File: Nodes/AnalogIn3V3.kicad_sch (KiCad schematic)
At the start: 20 parts, among them T19 Conn_01x01, T20 Conn_01x01, U10 LM358BAIDR

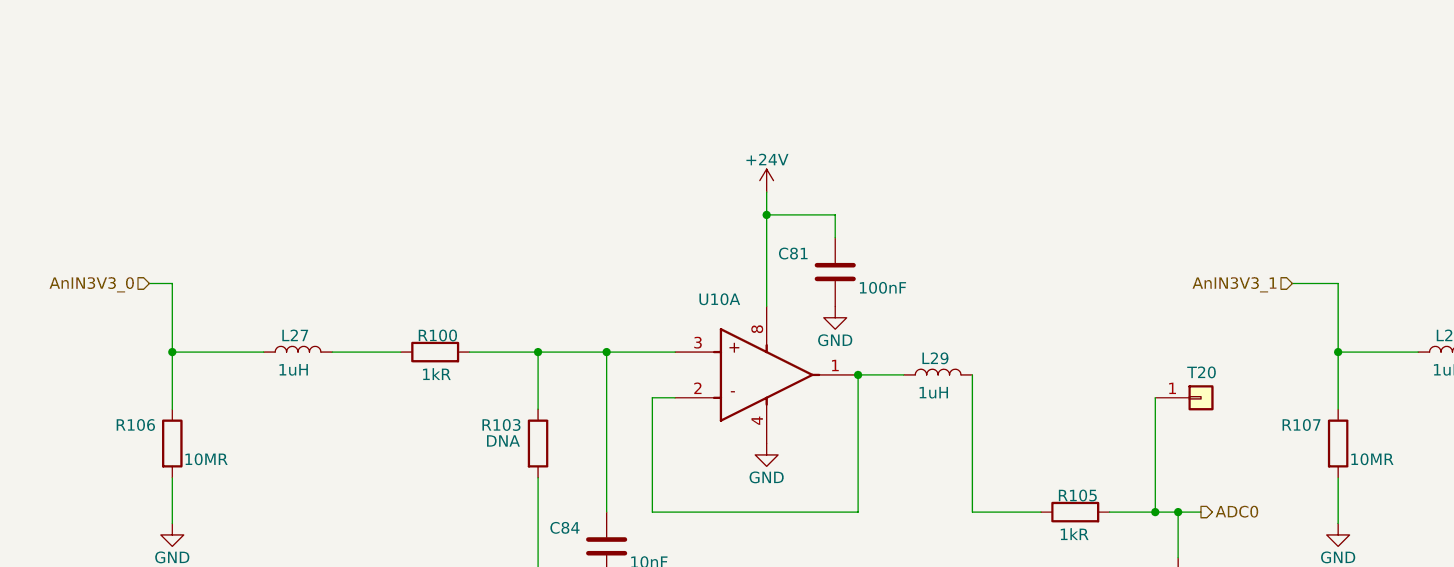
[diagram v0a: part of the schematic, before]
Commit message: Nodes v2.1.2 Improved
- Improved schematic design
- Added two 4.7 uF caps according to the datasheets of the microchips
- Other small changes
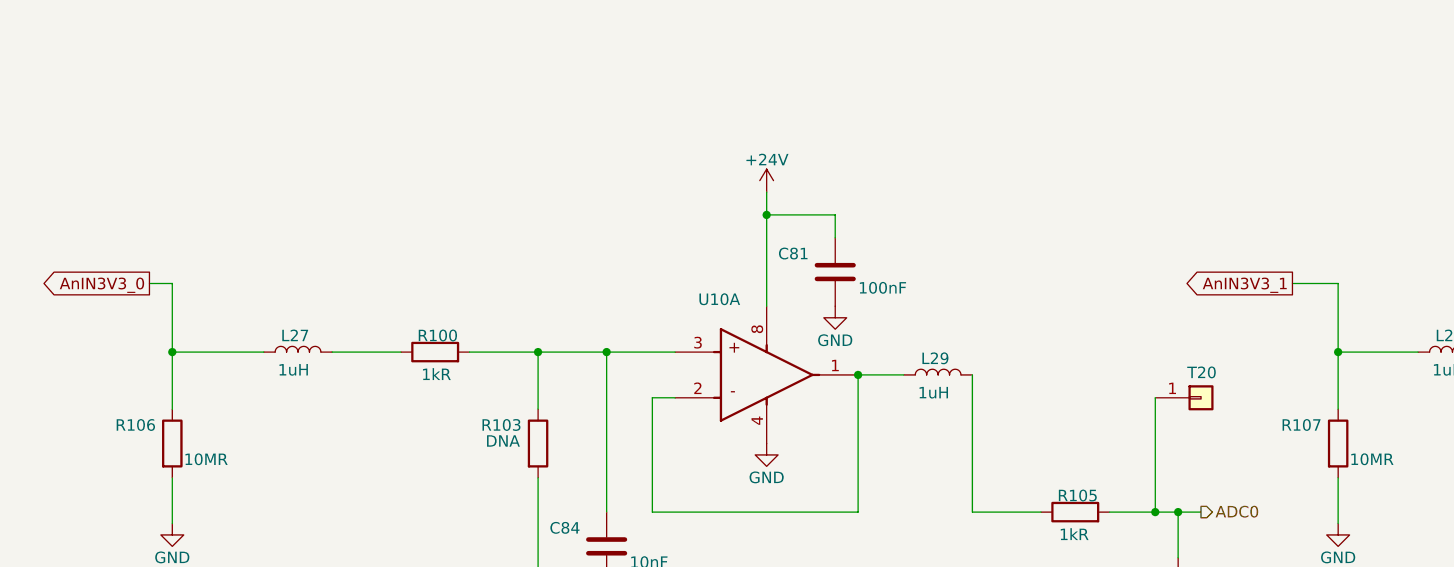
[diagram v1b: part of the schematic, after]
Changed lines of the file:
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@@
+		)
+	)
+	(global_label "AnIN3V3_1"
+		(shape output)
+		(at 151.13 62.23 180)
+		(fields_autoplaced yes)
+		(effects
+			(font
+				(size 1.27 1.27)
+			)
+			(justify right)
+		)
+		(property "Intersheetrefs" "${INTERSHEET_REFS}"
+			(at 138.2872 62.23 0)
+			(effects
+				(font
+					(size 1.27 1.27)
+				)
+				(justify right)
+				(hide yes)
+			)
+		)
+	)
+	(global_label "AnIN3V3_0"
+		(shape output)
+		(at 24.13 62.23 180)
+		(fields_autoplaced yes)
+		(effects
+			(font
+				(size 1.27 1.27)
+			)
+			(justify right)
+		)
+		(property "Intersheetrefs" "${INTERSHEET_REFS}"
+			(at 11.2872 62.23 0)
+			(effects
+				(font
+					(size 1.27 1.27)
+				)
+				(justify right)
+				(hide yes)
+			)
 		)
 	)
@@
 		)
 	)
-	(hierarchical_label "AnIN3V3_1"
-		(shape input)
-		(at 151.13 62.23 180)
-		(fields_autoplaced yes)
-		(effects
-			(font
-				(size 1.27 1.27)
-			)
-			(justify right)
-		)
-	)
-	(hierarchical_label "AnIN3V3_0"
-		(shape input)
-		(at 24.13 62.23 180)
-		(fields_autoplaced yes)
-		(effects
-			(font
-				(size 1.27 1.27)
-			)
-			(justify right)
-		)
-	)

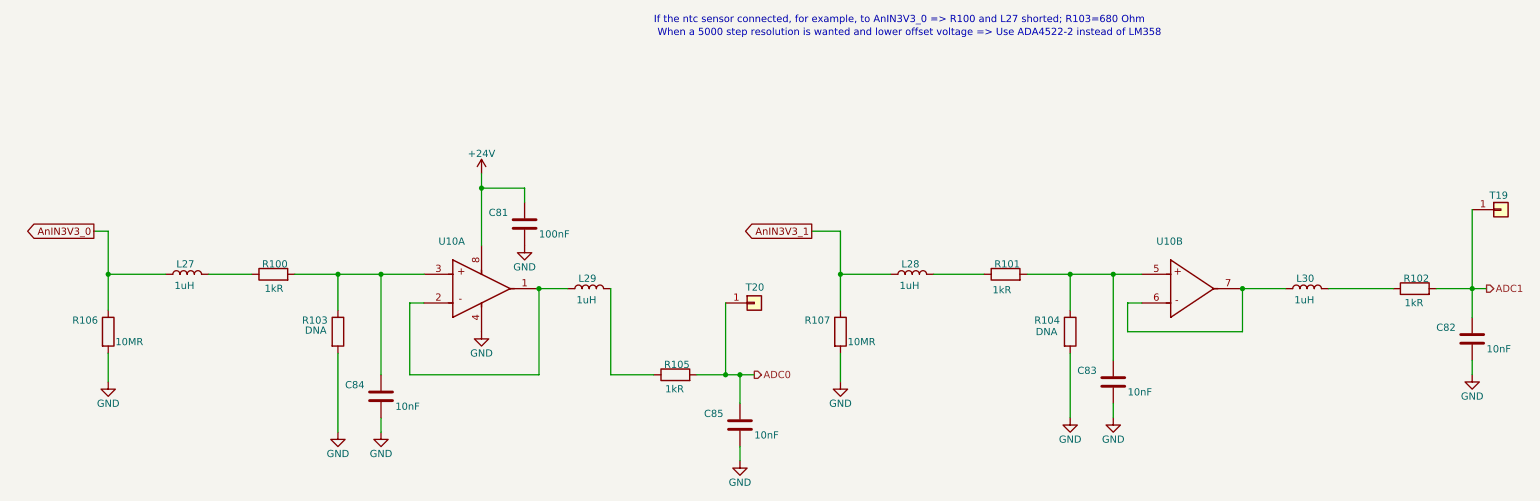
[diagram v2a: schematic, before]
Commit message: Nodes v2.2.5
- New High-Side Driver (Same footprint, just new info)
- Two resistors added for 3V3 Filters, which can be used to implement voltage divider
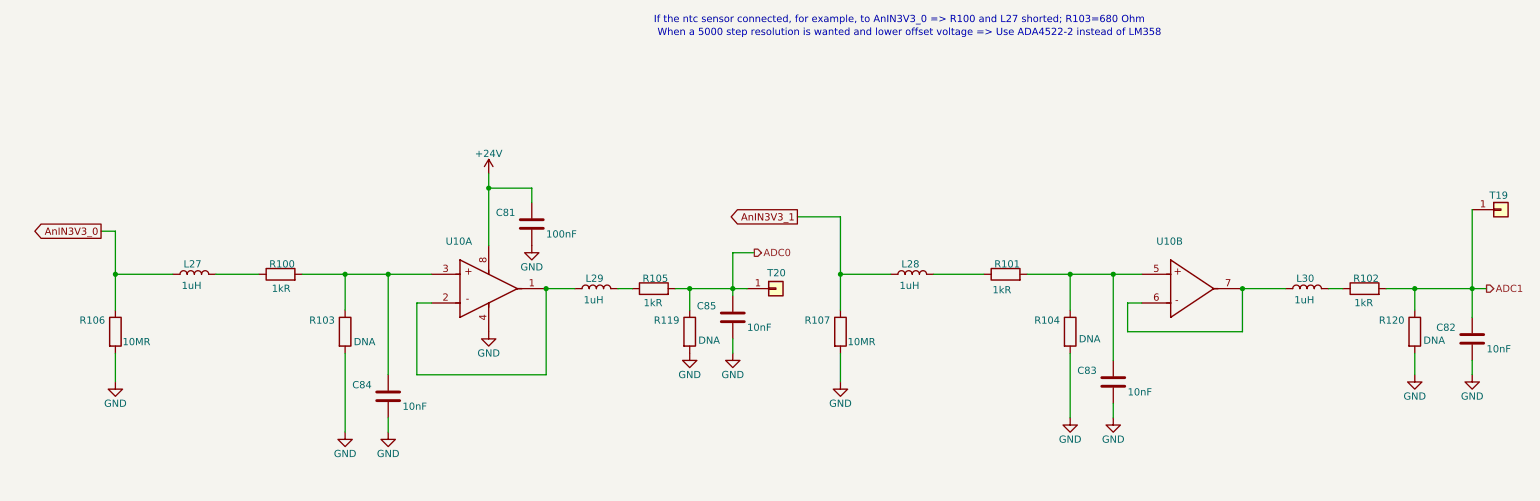
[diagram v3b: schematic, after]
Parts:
- added R119, R120: DNA, Resistor_SMD:R_0805_2012Metric_Pad1.20x1.40mm_HandSolder, symbol Device:R
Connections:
- net ADC0: now also R119.1
- net ADC1: now also R120.1
- net GND: now also R119.2, R120.2
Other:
- moved on the sheet: C81, C84, C85, L27, L29, R100, R102, R103, R105, R106, T20, U10A

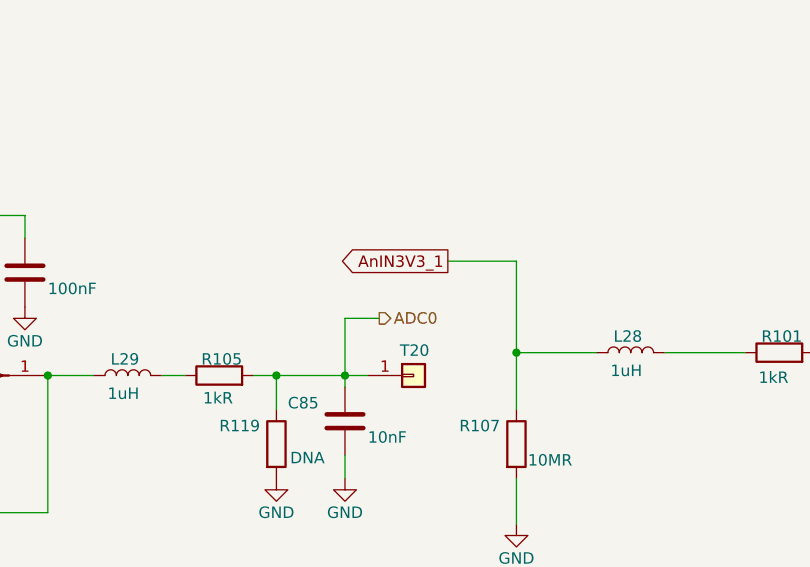
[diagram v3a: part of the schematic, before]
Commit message: Nodes 2.2.5 Revision 1
- New LED colour coding
- Nodes Datasheet added
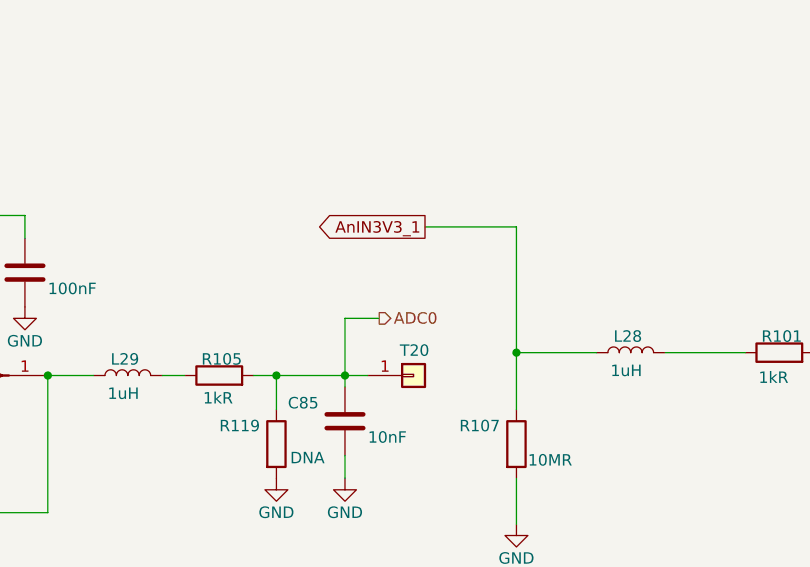
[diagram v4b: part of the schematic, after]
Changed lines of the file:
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@@
 	(wire
 		(pts
-			(xy 156.21 59.69) (xy 156.21 69.85)
+			(xy 156.21 55.88) (xy 156.21 69.85)
 		)
 		(stroke
@@
 	(wire
 		(pts
-			(xy 148.59 59.69) (xy 156.21 59.69)
+			(xy 146.05 55.88) (xy 156.21 55.88)
 		)
 		(stroke
@@
 	(global_label "AnIN3V3_1"
 		(shape output)
-		(at 148.59 59.69 180)
+		(at 146.05 55.88 180)
 		(fields_autoplaced yes)
 		(effects
@@
 		)
 		(property "Intersheetrefs" "${INTERSHEET_REFS}"
-			(at 135.7472 59.69 0)
+			(at 133.2072 55.88 0)
 			(effects
 				(font
